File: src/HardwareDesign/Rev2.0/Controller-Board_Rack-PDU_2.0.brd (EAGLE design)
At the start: 47 x 83 mm, 99 parts, among them IC1 W5500, IC2 RP2040, IC3 MCP6001R, IC4 W25Q128JVPIQ, IC5 MIC5504-3.3YM5-TR, IC6 CAT24C512HU5IGT3, X1 XC53M4-25.000-F18NJDTL, X2 K5A1200015304P

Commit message: source code - pre version. Never RP2040 or any RP series ever. Copiling to this is nightmare
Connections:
- net !INT renamed !W5500_INT
- net !RST renamed !W5500_RST
- net !SPI0_CS renamed !W5500_CS
- net SPI0_MISO renamed W5500_MISO
- net SPI0_MOSI renamed W5500_MOSI
- net SPI0_SCK renamed W5500_SCK
- net V_USB renamed ADC_V_USB
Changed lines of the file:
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@@
 <wire x1="26.11" y1="58.04" x2="27.57" y2="58.04" width="0.8128" layer="16"/>
 </signal>
-<signal name="SPI0_SCK">
+<signal name="W5500_SCK">
 <contactref element="IC2" pad="29"/>
 <contactref element="IC1" pad="33"/>
@@
 <wire x1="16.924" y1="42.64815625" x2="17.181078125" y2="42.391078125" width="0.2" layer="1"/>
 </signal>
-<signal name="SPI0_MISO">
+<signal name="W5500_MISO">
 <contactref element="IC2" pad="27"/>
 <contactref element="IC1" pad="34"/>
@@
 <wire x1="17.4622" y1="53.2078" x2="17.4622" y2="43.0678" width="0.2" layer="16"/>
 </signal>
-<signal name="SPI0_MOSI">
+<signal name="W5500_MOSI">
 <contactref element="IC2" pad="30"/>
 <contactref element="IC1" pad="35"/>
@@
 <wire x1="19.8483875" y1="53.13625" x2="18.3936375" y2="51.6815" width="0.2" layer="1"/>
 </signal>
-<signal name="!INT">
+<signal name="!W5500_INT">
 <contactref element="IC2" pad="32"/>
 <contactref element="IC1" pad="36"/>
@@
 <wire x1="40.1" y1="66.312" x2="40.1" y2="65.3" width="0.2" layer="1"/>
 </signal>
-<signal name="!RST">
+<signal name="!W5500_RST">
 <contactref element="IC2" pad="31"/>
 <contactref element="IC1" pad="37"/>
@@
 <wire x1="15.951" y1="45.251" x2="14.74" y2="44.04" width="0.2" layer="16"/>
 </signal>
-<signal name="!SPI0_CS">
+<signal name="!W5500_CS">
 <contactref element="IC2" pad="28"/>
 <contactref element="IC1" pad="32"/>
@@
 <wire x1="33.7076" y1="8.15" x2="33.7" y2="8.1424" width="0.6096" layer="1"/>
 </signal>
-<signal name="V_USB">
+<signal name="ADC_V_USB">
 <contactref element="R25" pad="2"/>
 <contactref element="R26" pad="1"/>

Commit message: correct findings
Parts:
- added R12, R29: 10K, ds_passive:0402
- R27: value 4.7K -> NC
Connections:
- net +3V3: now also R12.2, R29.2
- net MCP_DSP_RST: now also R12.1
- net MCP_REL_RST: now also R29.1
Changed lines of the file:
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@@
 <?xml version="1.0" encoding="utf-8"?>
 <!DOCTYPE eagle SYSTEM "eagle.dtd">
-<eagle version="9.2.1">
+<eagle version="9.6.2">
 <drawing>
 <settings>
@@
 </layers>
 <board>
-<fusionsync huburn="a.YnVzaW5lc3M6aG90bWFpbDE2OTAxNA" projecturn="a.YnVzaW5lc3M6aG90bWFpbDE2OTAxNCMyMDI1MDEwNTg1Mzg3MDcwMQ" f3durn="urn:adsk.wipprod:dm.lineage:k7dyHYkaTC204e2t4i2SaQ" pcbguid="422b6cc1-f17d-42d3-8275-fd1ae89a2870" lastpulledtime="" lastsyncedchangeguid="8fdbbd98-52c0-9c9a-ea3d-b20e171e31ce"/>
+<fusionsync huburn="a.YnVzaW5lc3M6aG90bWFpbDE2OTAxNA" projecturn="a.YnVzaW5lc3M6aG90bWFpbDE2OTAxNCMyMDI1MDEwNTg1Mzg3MDcwMQ" f3durn="urn:adsk.wipprod:dm.lineage:k7dyHYkaTC204e2t4i2SaQ" pcbguid="422b6cc1-f17d-42d3-8275-fd1ae89a2870" lastpulledtime="" lastsyncedchangeguid="8fdbbd98-52c0-9c9a-ea3d-b20e171e31ce" latestrevisionid="" lastsyncedrevisionid="" lastboardhashguid="" lastpushedtime="" linktopcb3d="false"/>
 <plain>
 <text x="1.67" y="6.88" size="1.27" layer="26" font="vector" ratio="13" rot="MR90">github.com/DvidMakesThings/HW_10-In-Rack_PDU
@@
 <attribute name="VALUE" x="26.829" y="14.151" size="1.016" layer="27" rot="R270"/>
 </element>
-<element name="R27" library="ds_passive" package="0402" package3d_urn="urn:adsk.eagle:package:46683744/2" value="4.7K" x="28.4072" y="73.2462" smashed="yes">
+<element name="R27" library="ds_passive" package="0402" package3d_urn="urn:adsk.eagle:package:46683744/2" value="NC" x="28.4072" y="73.2462" smashed="yes">
 <attribute name="NAME" x="27.1372" y="73.932" size="1.016" layer="25" rot="R180"/>
 <attribute name="VALUE" x="27.7722" y="71.3412" size="1.016" layer="27"/>
@@
 <attribute name="VALUE" x="19.122" y="78.4434" size="1.27" layer="27" rot="R180"/>
 </element>
+<element name="R12" library="ds_passive" package="0402" package3d_urn="urn:adsk.eagle:package:46683744/2" value="10K" x="-12.05" y="-5.96" smashed="yes">
+<attribute name="NAME" x="-12.685" y="-5.325" size="1.016" layer="25"/>
+<attribute name="VALUE" x="-12.685" y="-7.865" size="1.016" layer="27"/>
+</element>
+<element name="R29" library="ds_passive" package="0402" package3d_urn="urn:adsk.eagle:package:46683744/2" value="10K" x="-12.05" y="-10.48" smashed="yes">
+<attribute name="NAME" x="-12.685" y="-9.845" size="1.016" layer="25"/>
+<attribute name="VALUE" x="-12.685" y="-12.385" size="1.016" layer="27"/>
+</element>
 </elements>
 <signals>
@@
 <wire x1="35.84" y1="41.0842" x2="35.84" y2="41.14" width="0.4064" layer="16"/>
 <wire x1="35.84" y1="41.14" x2="35.47" y2="41.51" width="0.4064" layer="16"/>
+<contactref element="R12" pad="2"/>
+<contactref element="R29" pad="2"/>
+<wire x1="-11.4" y1="-5.96" x2="-11.4" y2="-10.48" width="0" layer="19" extent="1-1"/>
+<wire x1="10.625" y1="5.29" x2="-11.4" y2="-5.96" width="0" layer="19" extent="1-1"/>
 </signal>
 <signal name="GND">
@@
 <wire x1="10.38" y1="14.22" x2="11.6254" y2="15.4654" width="0.2032" layer="1"/>
 <wire x1="11.6254" y1="15.4654" x2="11.6254" y2="17.73" width="0.2032" layer="1"/>
+<contactref element="R12" pad="1"/>
+<wire x1="4.7" y1="10.95" x2="-12.7" y2="-5.96" width="0" layer="19" extent="1-1"/>
 </signal>
 <signal name="MCP_REL_RST">
@@
 <wire x1="6.27" y1="36.05" x2="4.7" y2="36.05" width="0.2032" layer="1"/>
 <wire x1="7.138" y1="52.2266" x2="7.138" y2="36.918" width="0.2032" layer="16"/>
+<contactref element="R29" pad="1"/>
+<wire x1="-12.7" y1="-10.48" x2="4.7" y2="36.05" width="0" layer="19" extent="1-1"/>
 </signal>
 <signal name="LCD_CS">

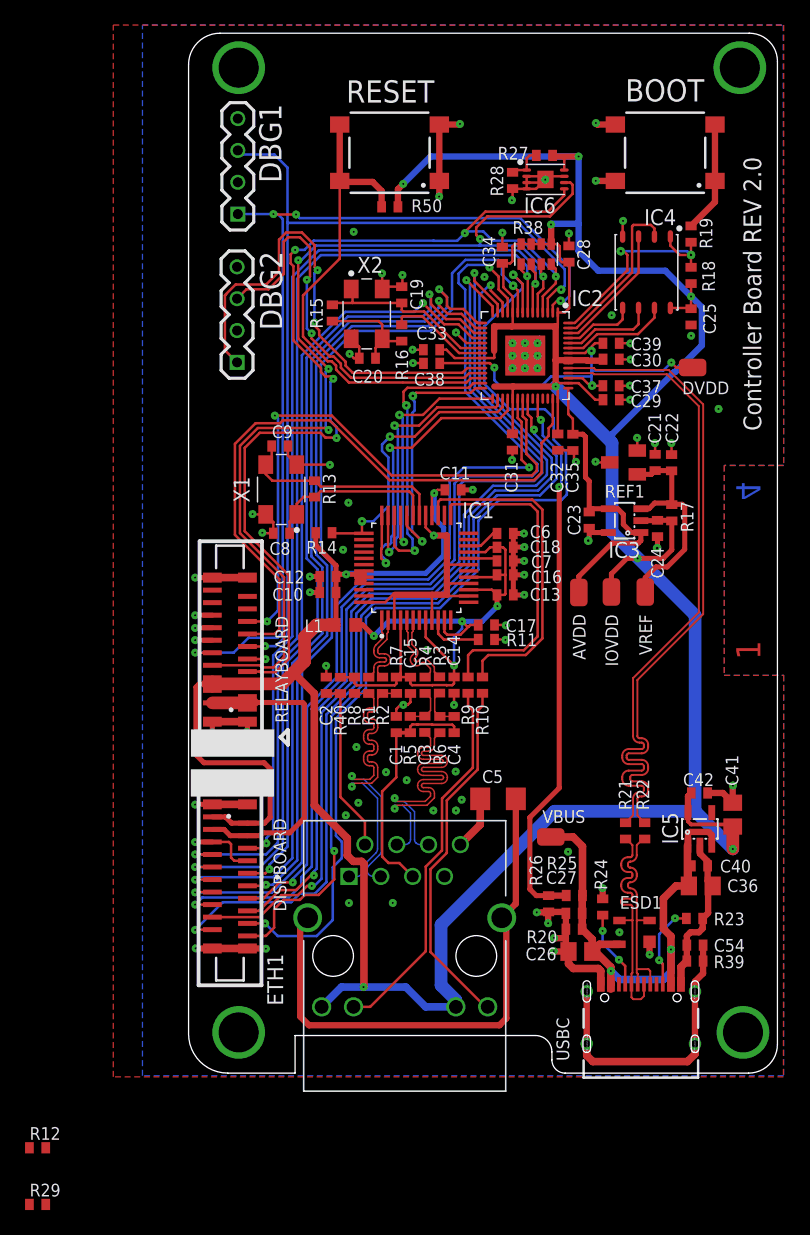
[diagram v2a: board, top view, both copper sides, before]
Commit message: I2C, SPI-DMA, EEPROM driver ready
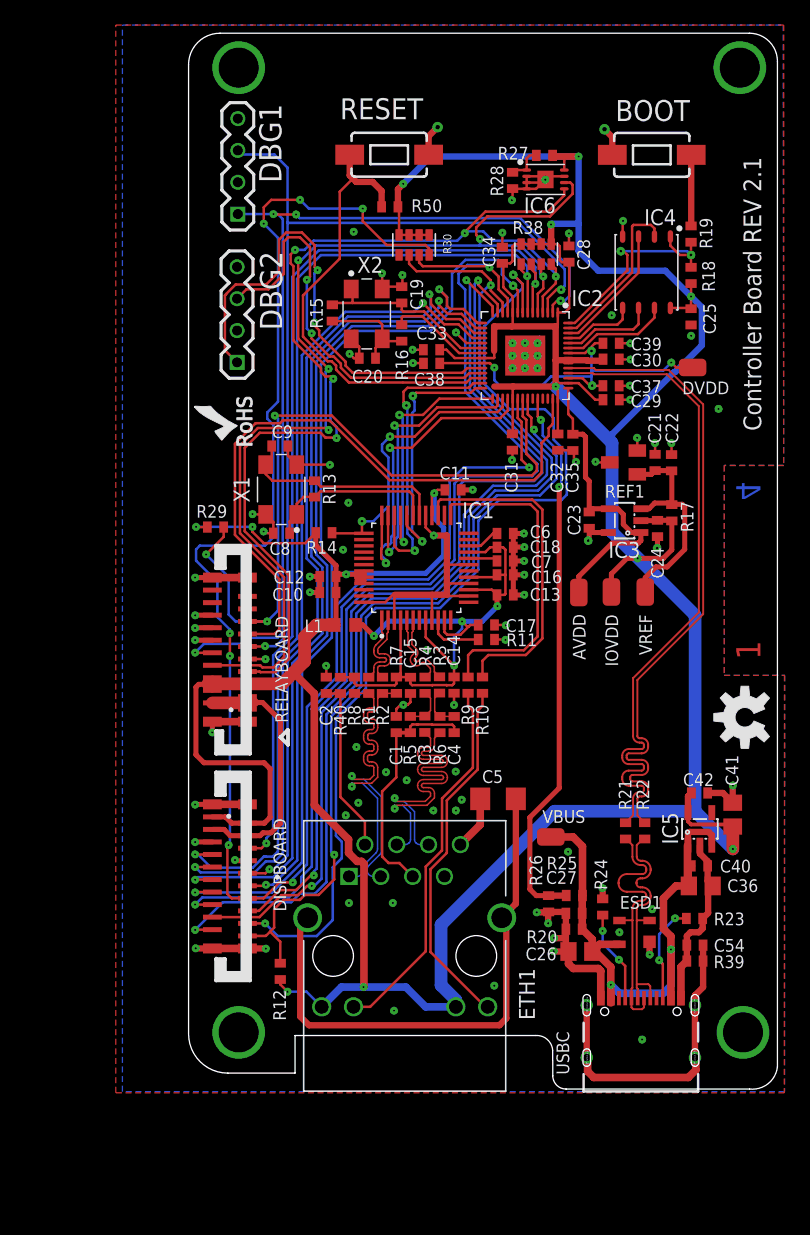
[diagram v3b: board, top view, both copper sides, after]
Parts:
- added R30: 4D03WGJ0332T5E, Resistor Array:742C083103JP
- added U$2: (no value), SparkFun-Aesthetics:OSHW-LOGO-M
- added U$3: (no value), SparkFun-Aesthetics:ROHS_LOGO_0.18_IN
- BOOT, RESET: value 430182043816 -> RS032G05A3SM-SPST-MOMENTARY-SWSMD-1101NE; device Wurth_Switch_WS-TASV:430182043816 -> BeagleBone_Blue_R3:TACTILE-SWITCH-1101NE
- moved R29 55.9 mm to (2.15, 43.6), turned to 180 degrees
- moved R12 23.9 mm to (7.32, 8.12), turned to 270 degrees
- moved USBC 1.10 mm to (36.1, 1.24)
- moved BOOT 1.08 mm to (37.0, 73.3)
- moved RESET 0.16 mm to (16.0, 73.3)
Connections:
- net +3V3: now also R30.1, R30.2, R30.3, R30.4
- net GND: now also BOOT.2; no longer BOOT.3, BOOT.4, RESET.2
- net LCD_CS: now also R30.6
- net LCD_MISO: now also R30.7
- net LCD_RES: now also R30.8
- net N$17: now also RESET.2; no longer RESET.3, RESET.4
- net USB_BOOT: no longer BOOT.2
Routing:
- net LCD_RES: track 57.1 -> 137.6 mm, vias 2 -> 8
- net +3V3: track 321.2 -> 341.7 mm, vias 10 -> 13
- net MCP_REL_RST: track 47.7 -> 59.3 mm, vias 2 -> 3
- net LCD_CS: track 79.0 -> 87.1 mm
- net GND: track 182.0 -> 175.3 mm, vias 96 -> 98
- net LCD_MISO: track 83.1 -> 89.5 mm
- net +5V: track 25.6 -> 21.3 mm
- net VBUS: track 44.2 -> 47.5 mm
- net USB_BOOT: track 8.88 -> 5.68 mm
- net MCP_DSP_RST: track 61.5 -> 64.4 mm
- net N$17: track 39.2 -> 36.4 mm
- net DP_P: track 16.4 -> 18.4 mm
- net DP_N: track 19.4 -> 21.0 mm
- net USB_SHIELD: track 23.2 -> 24.7 mm
- net I2C0_SCL: track 78.5 -> 79.8 mm
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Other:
- board size 47 x 83 mm -> 47 x 84.3 mm
- board text added: "Controller Board REV 2.1"
- board text removed: "Controller Board REV 2.0"
